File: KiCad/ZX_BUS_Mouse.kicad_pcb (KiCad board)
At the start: 2 copper layers, 99.1 x 40 mm, 28 parts, among them J1 X1A, J2 X1B, J4 Mini-DIN-6, J5 Conn_02x03_Odd_Even ISP, J6 Conn_01x04 Debug, J7 Conn_02x05_Odd_Even JTAG, U1 ATmega8A-A, U2 EPM3032ALC44, U3 AMS1117-3.3

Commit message: Fix PCB backface ZX-BUS pins silkscreen labels.
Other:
- board text added: "*A0"
- board text added: "*A1"
- board text added: "*A11"
- board text added: "*A12"
- board text added: "*A14"
- board text added: "*A2"
- board text added: "*A3"
- board text added: "*A4"
- board text added: "*A5"
- board text added: "*A6"
- board text added: "*A7"
- board text added: "*A9"
- board text added: "*BSAK/"
- board text added: "*BSRQ/"
- board text added: "*RST/"
- board text added: "+5V"
- board text added: "+5V_1"
- board text added: "CLK"
- board text added: "CSROM/"
- board text added: "DOS/"
- board text added: "F14M"
- board text added: "IOGE/"
- board text added: "NU0"
- board text added: "NU1"
- board text added: "RDR/"
- board text added: "RS/"
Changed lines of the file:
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@@
   (gr_line (start 132.08 142.875) (end 130.175 142.875)
     (stroke (width 0.1) (type solid)) (layer "Edge.Cuts"))
-  (gr_text "*D3" (at 79.375 139.065 90) (layer "B.SilkS")
+  (gr_text "*A2" (at 79.375 139.065 90) (layer "B.SilkS")
     (effects (font (size 1 0.9) (thickness 0.15)) (justify mirror))
   )
-  (gr_text "*D4" (at 81.915 139.065 90) (layer "B.SilkS")
+  (gr_text "*A3" (at 81.915 139.065 90) (layer "B.SilkS")
     (effects (font (size 1 0.9) (thickness 0.15)) (justify mirror))
   )
-  (gr_text "*A8" (at 117.475 139.065 90) (layer "B.SilkS")
+  (gr_text "*BSAK/" (at 117.475 138.6 90) (layer "B.SilkS")
     (effects (font (size 1 0.8) (thickness 0.15)) (justify mirror))
   )
-  (gr_text "MREQ/" (at 92.075 139.065 90) (layer "B.SilkS")
-    (effects (font (size 1 0.7) (thickness 0.15)) (justify mirror))
+  (gr_text "RS/" (at 92.075 139.065 90) (layer "B.SilkS")
+    (effects (font (size 1 0.9) (thickness 0.15)) (justify mirror))
   )
-  (gr_text "NU4" (at 109.855 139.065 90) (layer "B.SilkS")
+  (gr_text "*A5" (at 109.855 139.065 90) (layer "B.SilkS")
+    (effects (font (size 1 0.9) (thickness 0.15)) (justify mirror))
+  )
+  (gr_text "NU1" (at 97.155 139.065 90) (layer "B.SilkS")
+    (effects (font (size 1 0.9) (thickness 0.15)) (justify mirror))
+  )
+  (gr_text "*A12" (at 56.515 139.065 90) (layer "B.SilkS")
+    (effects (font (size 1 0.9) (thickness 0.15)) (justify mirror))
+  )
+  (gr_text "*BSRQ/" (at 99.7 138.5 90) (layer "B.SilkS")
     (effects (font (size 1 0.8) (thickness 0.15)) (justify mirror))
   )
-  (gr_text "*RD/" (at 97.155 139.065 90) (layer "B.SilkS")
+  (gr_text "+5V_1" (at 125.095 139 90) (layer "B.SilkS")
+    (effects (font (size 1 0.8) (thickness 0.15)) (justify mirror))
+  )
+  (gr_text "GND" (at 127.635 139.065 90) (layer "B.SilkS")
     (effects (font (size 1 0.9) (thickness 0.15)) (justify mirror))
   )
-  (gr_text "*A13" (at 56.515 139.065 90) (layer "B.SilkS")
-    (effects (font (size 1 0.8) (thickness 0.15)) (justify mirror))
-  )
-  (gr_text "*WR/" (at 99.695 139.065 90) (layer "B.SilkS")
+  (gr_text "GND" (at 69.215 139.065 90) (layer "B.SilkS")
     (effects (font (size 1 0.9) (thickness 0.15)) (justify mirror))
   )
-  (gr_text "+12V_1" (at 125.095 139.065 90) (layer "B.SilkS")
-    (effects (font (size 1 0.7) (thickness 0.15)) (justify mirror))
-  )
-  (gr_text "GND" (at 127.635 139.065 90) (layer "B.SilkS")
-    (effects (font (size 1 0.8) (thickness 0.15)) (justify mirror))
-  )
-  (gr_text "*D1" (at 69.215 139.065 90) (layer "B.SilkS")
+  (gr_text "IOGE/" (at 84.455 138.8 90) (layer "B.SilkS")
     (effects (font (size 1 0.9) (thickness 0.15)) (justify mirror))
   )
-  (gr_text "*INT/" (at 84.455 139.065 90) (layer "B.SilkS")
-    (effects (font (size 1 0.8) (thickness 0.15)) (justify mirror))
-  )
-  (gr_text "IORQ/" (at 94.615 139.065 90) (layer "B.SilkS")
-    (effects (font (size 1 0.7) (thickness 0.15)) (justify mirror))
-  )
-  (gr_text "*D6" (at 74.295 139.065 90) (layer "B.SilkS")
+  (gr_text "NU0" (at 94.615 139.065 90) (layer "B.SilkS")
     (effects (font (size 1 0.9) (thickness 0.15)) (justify mirror))
   )
-  (gr_text "TURBO" (at 64.135 139.065 90) (layer "B.SilkS")
-    (effects (font (size 1 0.7) (thickness 0.15)) (justify mirror))
-  )
-  (gr_text "*A15" (at 53.975 139.065 90) (layer "B.SilkS")
-    (effects (font (size 1 0.8) (thickness 0.15)) (justify mirror))
-  )
-  (gr_text "BLK" (at 61.595 139.065 90) (layer "B.SilkS")
+  (gr_text "*A0" (at 74.295 139.065 90) (layer "B.SilkS")
     (effects (font (size 1 0.9) (thickness 0.15)) (justify mirror))
   )
-  (gr_text "NU3" (at 107.315 139.065 90) (layer "B.SilkS")
-    (effects (font (size 1 0.8) (thickness 0.15)) (justify mirror))
-  )
-  (gr_text "*D0" (at 66.675 139.065 90) (layer "B.SilkS")
+  (gr_text "F14M" (at 64.135 139.065 90) (layer "B.SilkS")
     (effects (font (size 1 0.9) (thickness 0.15)) (justify mirror))
   )
-  (gr_text "*D2" (at 71.755 139.065 90) (layer "B.SilkS")
+  (gr_text "*A14" (at 53.975 139.065 90) (layer "B.SilkS")
+    (effects (font (size 1 0.9) (thickness 0.15)) (justify mirror))
+  )
+  (gr_text "DOS/" (at 61.595 139.065 90) (layer "B.SilkS")
+    (effects (font (size 1 0.9) (thickness 0.15)) (justify mirror))
+  )
+  (gr_text "*A6" (at 107.315 139.065 90) (layer "B.SilkS")
+    (effects (font (size 1 0.9) (thickness 0.15)) (justify mirror))
+  )
+  (gr_text "GND" (at 66.675 139.065 90) (layer "B.SilkS")
+    (effects (font (size 1 0.9) (thickness 0.15)) (justify mirror))
+  )
+  (gr_text "CLK" (at 71.755 139.065 90) (layer "B.SilkS")
     (effects (font (size 1 0.9) (thickness 0.15)) (justify mirror))
   )
@@
     (effects (font (size 1.2 1.2) (thickness 0.17)) (justify left bottom mirror))
   )
-  (gr_text "*HLT/" (at 89.535 139.065 90) (layer "B.SilkS")
+  (gr_text "RDR/" (at 89.535 139 90) (layer "B.SilkS")
+    (effects (font (size 1 0.9) (thickness 0.15)) (justify mirror))
+  )
+  (gr_text "*A4" (at 112.395 139.065 90) (layer "B.SilkS")
+    (effects (font (size 1 0.9) (thickness 0.15)) (justify mirror))
+  )
+  (gr_text "*A11" (at 122.555 139.065 90) (layer "B.SilkS")
+    (effects (font (size 1 0.9) (thickness 0.15)) (justify mirror))
+  )
+  (gr_text "*RST/" (at 102.235 139.065 90) (layer "B.SilkS")
     (effects (font (size 1 0.8) (thickness 0.15)) (justify mirror))
   )
-  (gr_text "*M1/" (at 112.395 139.065 90) (layer "B.SilkS")
+  (gr_text "CSROM/" (at 114.935 138.4 90) (layer "B.SilkS")
     (effects (font (size 1 0.8) (thickness 0.15)) (justify mirror))
-  )
-  (gr_text "+5V_2" (at 122.555 139.065 90) (layer "B.SilkS")
-    (effects (font (size 1 0.8) (thickness 0.15)) (justify mirror))
-  )
-  (gr_text "NU2" (at 102.235 139.065 90) (layer "B.SilkS")
-    (effects (font (size 1 0.8) (thickness 0.15)) (justify mirror))
-  )
-  (gr_text "*RFSH/" (at 114.935 139.065 90) (layer "B.SilkS")
-    (effects (font (size 1 0.7) (thickness 0.15)) (justify mirror))
   )
   (gr_text "github.com/proboterror/ZX_BUS_Mouse" (at 93.4 127.4) (layer "B.SilkS")
     (effects (font (size 1 1) (thickness 0.15)) (justify left bottom mirror))
   )
-  (gr_text "*D7" (at 59.055 139.065 90) (layer "B.SilkS")
+  (gr_text "+5V" (at 59.055 139.065 90) (layer "B.SilkS")
     (effects (font (size 1 0.9) (thickness 0.15)) (justify mirror))
   )
-  (gr_text "*NMI/" (at 86.995 139.065 90) (layer "B.SilkS")
-    (effects (font (size 1 0.8) (thickness 0.15)) (justify mirror))
-  )
-  (gr_text "*D5" (at 76.835 139.065 90) (layer "B.SilkS")
+  (gr_text "GND" (at 86.995 139.065 90) (layer "B.SilkS")
     (effects (font (size 1 0.9) (thickness 0.15)) (justify mirror))
   )
-  (gr_text "*WAIT/" (at 104.775 139.065 90) (layer "B.SilkS")
-    (effects (font (size 1 0.7) (thickness 0.15)) (justify mirror))
+  (gr_text "*A1" (at 76.835 139.065 90) (layer "B.SilkS")
+    (effects (font (size 1 0.9) (thickness 0.15)) (justify mirror))
   )
-  (gr_text "*A10" (at 120.015 139.065 90) (layer "B.SilkS")
-    (effects (font (size 1 0.8) (thickness 0.15)) (justify mirror))
+  (gr_text "*A7" (at 104.775 139.065 90) (layer "B.SilkS")
+    (effects (font (size 1 0.9) (thickness 0.15)) (justify mirror))
+  )
+  (gr_text "*A9" (at 120.015 139.065 90) (layer "B.SilkS")
+    (effects (font (size 1 0.9) (thickness 0.15)) (justify mirror))
   )
   (gr_text "BLK" (at 61.595 139.065 90) (layer "F.SilkS")

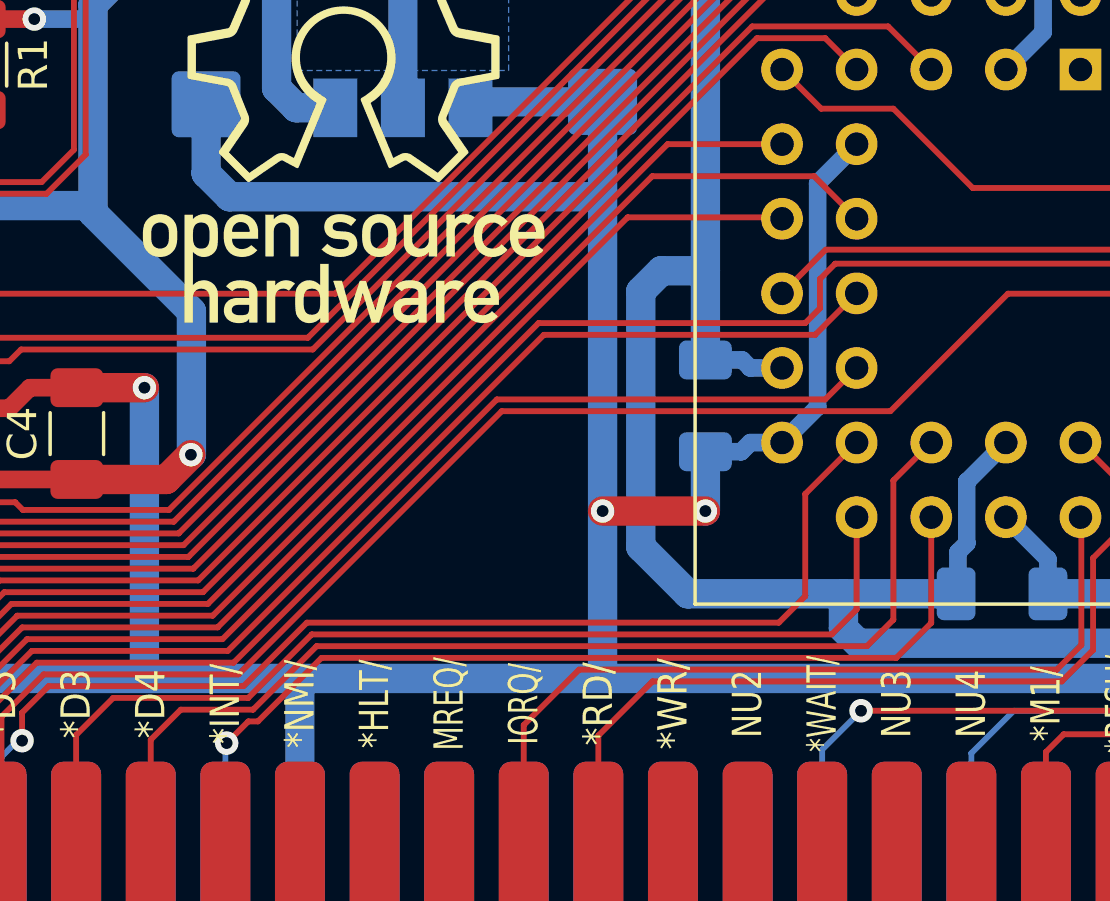
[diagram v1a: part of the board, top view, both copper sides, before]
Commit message: Add 74LVC1G125DB 3-state buffer for IORQGE/IOGE signal: 5V output signal level. Resolve issue with ZX-BUS XTRaiser, prevent potential issues with 5V IORQGE back current from other cards to CPLD output pin. Change CPLD IORQGE output logic to 2-state. Swap D3/D4 CPLD pins.
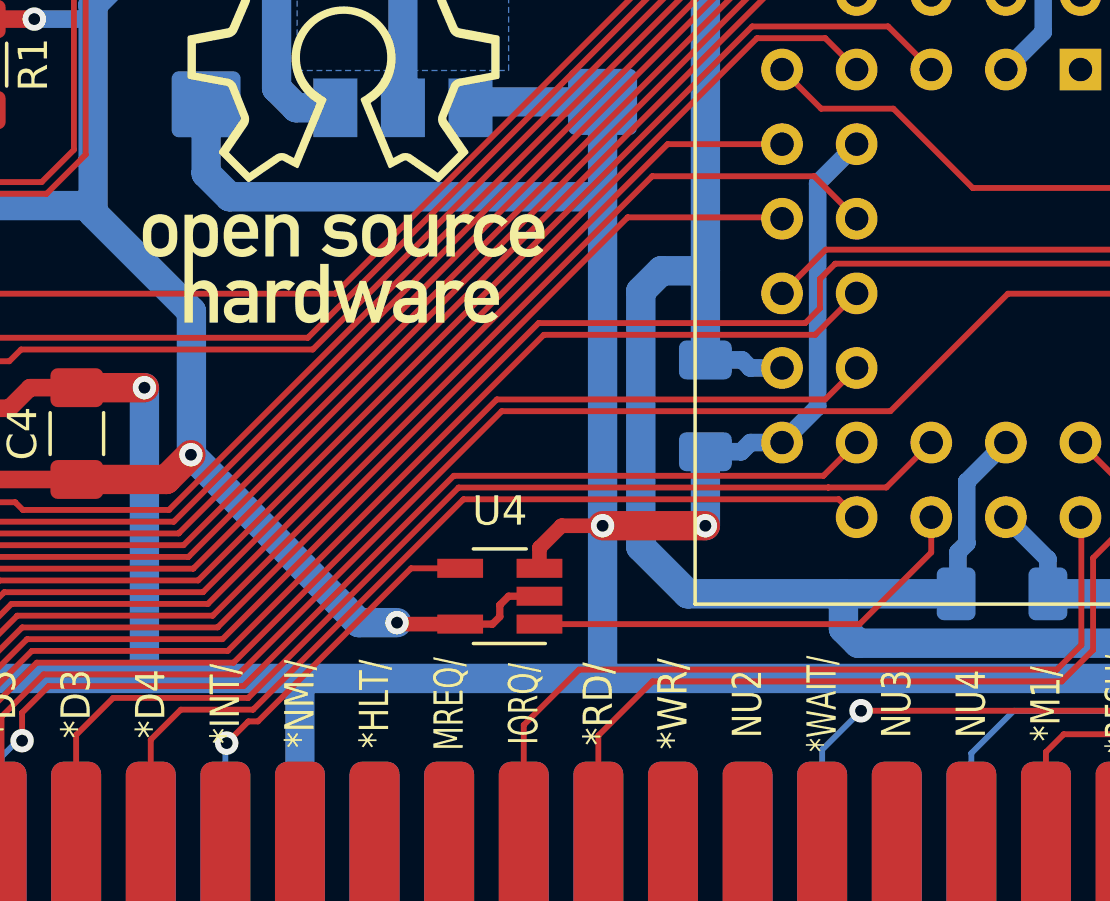
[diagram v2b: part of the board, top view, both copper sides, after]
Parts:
- added U4: 74LVC1G125, Package_TO_SOT_SMD:SOT-23-5_HandSoldering, F.Cu at (93.8, 135.4)
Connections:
- U2 pad 18: /*D3 -> /*D4
- U2 pad 20: /IOGE/ -> /IORQGE/
- U2 pad 21: /*D4 -> /*D3
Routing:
- net /IOGE/: track 33.9 -> 15.1 mm
- net /IORQGE/: track 0.00 -> 15.6 mm
- net VCC: track 145.3 -> 160.2 mm, vias 6 -> 7
- net /*D4: track 38.3 -> 32.4 mm
- net GND: track 500.0 -> 503.7 mm
- net /*A1: track 40.3 -> 38.3 mm
- net /*D3: track 36.4 -> 38.1 mm

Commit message: Add external PS/2 mouse bracket connector (common 486-Pentium AT motherboards pinout). Add debug UART connector (RX/TX). Move I2C debug connector, move optional R8, R9 pullup resistors to backside. Change Mini DIN connector drill holes diameter from 0.8 to 0.9 mm. Alter silkscreen labels.
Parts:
- added J3: UART, Connector_PinHeader_2.54mm:PinHeader_1x02_P2.54mm_Vertical, F.Cu at (76.3, 123.8)
- added J8: PS/2 External Bracket, Connector_PinHeader_2.54mm:PinHeader_2x04_P2.54mm_Vertical, F.Cu at (57.4, 113.4)
- J5: value Conn_02x03_Odd_Even ISP -> ISP
- J6: value Conn_01x04 Debug -> Debug
- J7: value Conn_02x05_Odd_Even JTAG -> JTAG
- R8, R9: moved to B.Cu
- U4: value 74LVC1G125 -> 74LVC1G125DB
- moved R8 21.2 mm to (72.6, 117.2), turned to 90 degrees
- moved J6 21.2 mm to (79.5, 112.9)
- moved R9 18.4 mm to (76.1, 117.2), turned to 90 degrees
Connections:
- U1 pad 30: unconnected-(U1-PD0-Pad30) -> /RX
- U1 pad 31: unconnected-(U1-PD1-Pad31) -> /TX
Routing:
- net /SCL: track 47.5 -> 24.1 mm
- net /SDA: track 51.7 -> 28.5 mm
- net /MDAT: track 25.2 -> 40.8 mm
- net /TX: track 0.00 -> 14.5 mm, vias 0 -> 1
- net /RX: track 0.00 -> 9.90 mm, vias 0 -> 1
- net /MCLK: track 38.4 -> 44.7 mm
- net GND: track 503.7 -> 505.7 mm
- net VCC: track 160.2 -> 160.8 mm, vias 7 -> 6
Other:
- board text added: "DAT"
- board text added: "ISP"
- board text added: "PS/2 EXT"
- board text added: "RX"
- board text added: "TX"
- board text added: "UART"
